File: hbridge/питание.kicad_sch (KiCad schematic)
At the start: 8 parts, among them J19 24V, U14 AMS1117 3.3, U20 B2412S-2WR3, U4 AM6TW-2415DZ, U9 AM6TW-2415DZ

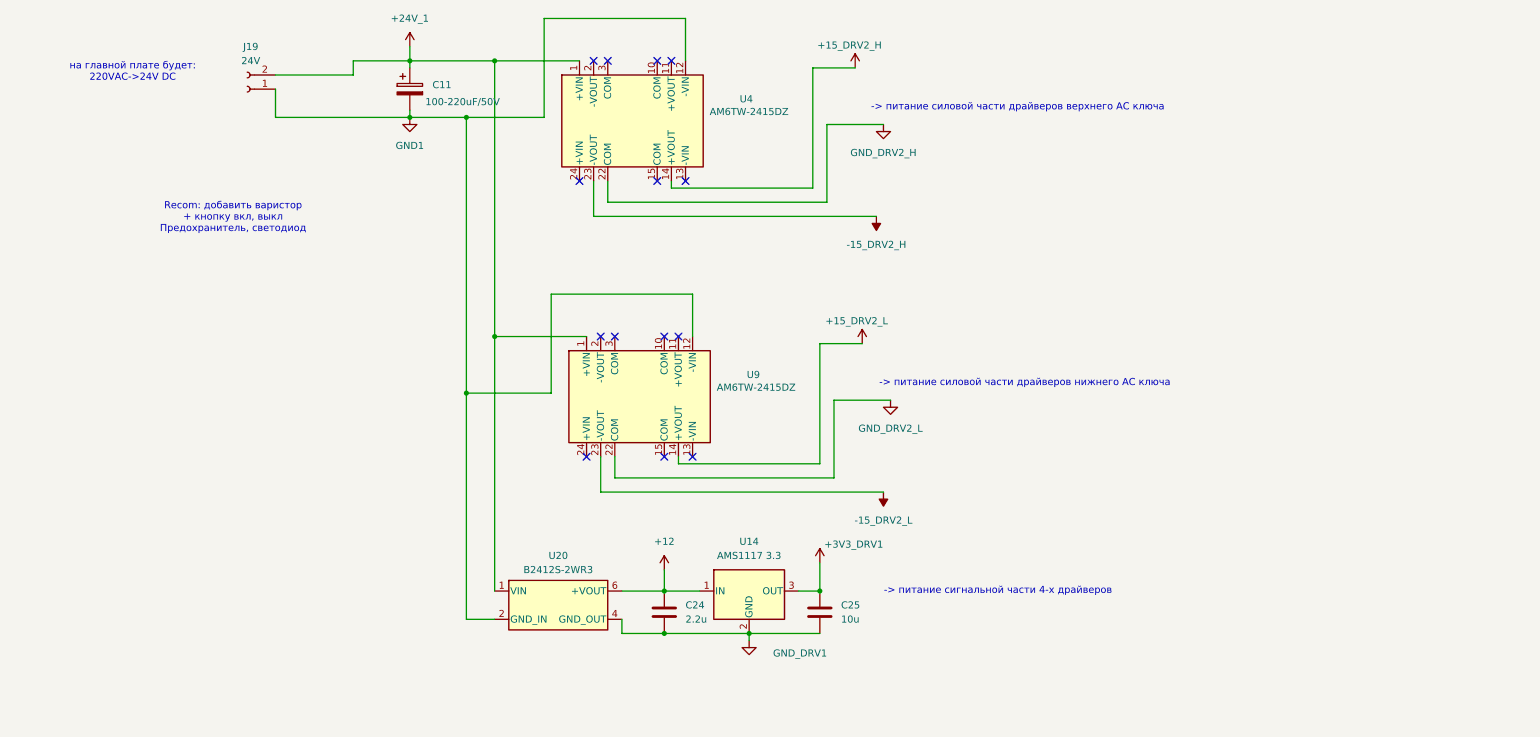
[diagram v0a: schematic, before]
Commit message: Half bridge power to PCB added.
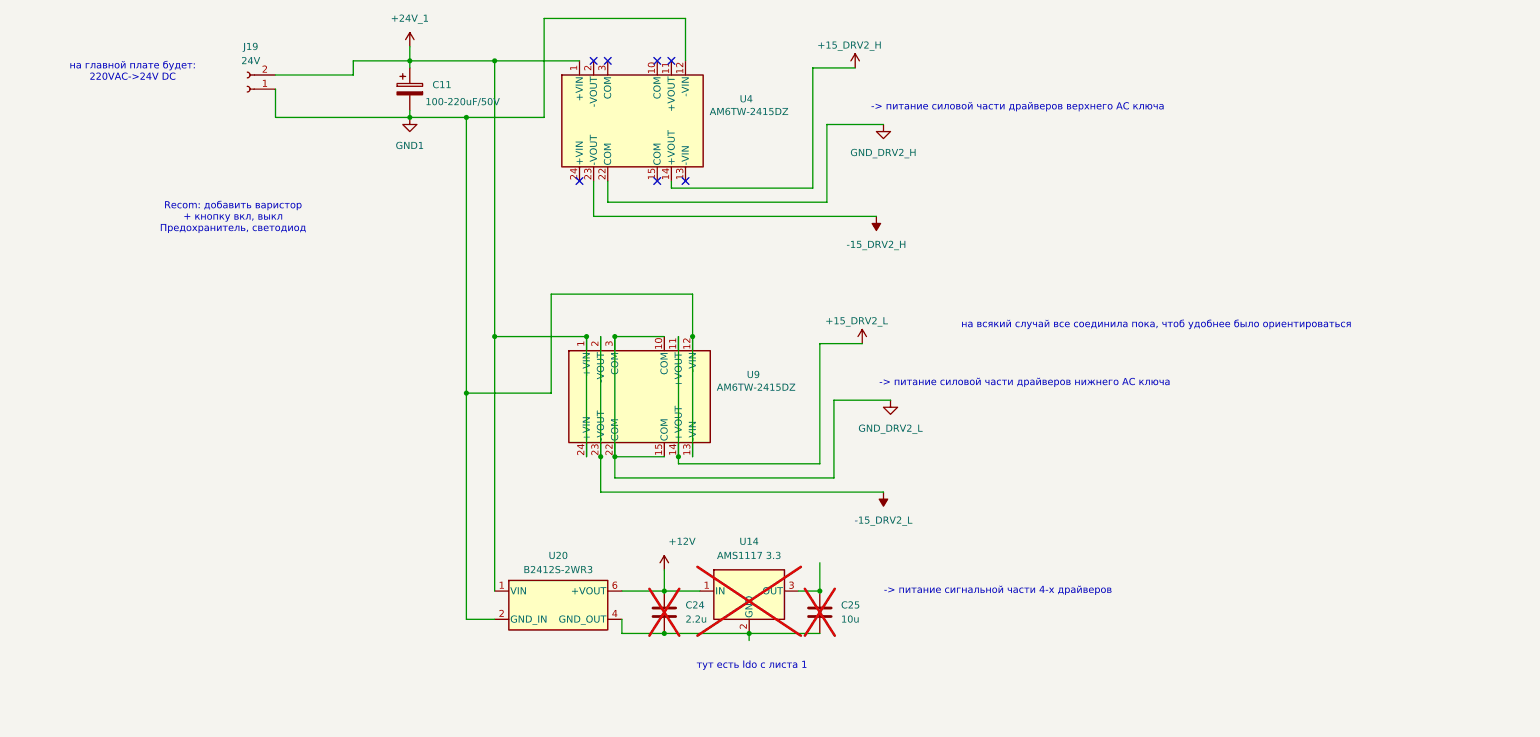
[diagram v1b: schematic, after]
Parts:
- C11: footprint (none) -> Capacitor_THT:CP_Radial_D7.5mm_P2.50mm
- C24, C25: footprint (none) -> Capacitor_SMD:C_0805_2012Metric_Pad1.18x1.45mm_HandSolder; now not fitted; now left out of the parts list
- J19: footprint TerminalBlock_Phoenix:TerminalBlock_Phoenix_MPT-0,5-2-2.54_1x02_P2.54mm_Horizontal -> TerminalBlock:TerminalBlock_Xinya_XY308-2.54-2P_1x02_P2.54mm_Horizontal
- U14: footprint (none) -> Package_TO_SOT_SMD:SOT-223; now not fitted; now left out of the parts list
- U20: footprint (none) -> TerminalBlock:TerminalBlock_Xinya_XY308-2.54-6P_1x06_P2.54mm_Horizontal
- U4, U9: footprint (none) -> Package_DIP:DIP-24_18.0mmx34.29mm_W15.24mm_LongPads
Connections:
- net +15_DRV2_L: now also U9.11 (+VOUT)
- net +24V_1: now also U9.24 (+VIN)
- net -15_DRV2_L: now also U9.2 (-VOUT)
- net GND1: now also U9.13 (-VIN)
- net GND_DRV2_L: now also U9.10 (COM), U9.15 (COM), U9.3 (COM)
- net +12 renamed +12V
- net +3V3_DRV1: no longer names the net of C25.1, U14.3 (OUT)
- net GND_DRV1: no longer names the net of C24.2, C25.2, U14.2 (GND), U20.4 (GND_OUT)
- no-connect marks 14 -> 7
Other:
- note added: "на всякий случай все соединила пока, чтоб удобнее было ориентироваться"
- note added: "тут есть ldo с листа 1"

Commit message: Half-bridge, no MCU.
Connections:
- net +15_DRV2_L: no longer U9.14 (+VOUT)
- net +24V_1: no longer U9.1 (+VIN)
- net -15_DRV2_L: no longer U9.23 (-VOUT)
- net GND1: no longer U9.12 (-VIN)
- net GND_DRV2_H: now also U4.3 (COM); no longer U4.22 (COM)
- net GND_DRV2_L: no longer U9.10 (COM), U9.15 (COM), U9.3 (COM)
- net GND_DRV1: now reaches C24.2, C25.2, U14.2 (GND), U20.4 (GND_OUT)
- no-connect marks 7 -> 14
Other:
- note removed: "на всякий случай все соединила пока, чтоб удобнее было ориентироваться"

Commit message: Hierarchy changed. MCU optocouplers started.
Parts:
- renumbered C25 to C2, C24 to C4, U14 to U7
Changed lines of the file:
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@@
 		(instances
 			(project "hbridge"
-				(path "/2ca728bc-601a-44e1-8d59-41d5093f57eb"
+				(path "/96bc687b-1f0f-4b2f-95bf-a0725acd0403/5c304d23-1a3b-43ed-8f7a-219a4f2f60a2"
 					(reference "#PWR08")
 					(unit 1)
@@
 		(instances
 			(project "hbridge"
-				(path "/2ca728bc-601a-44e1-8d59-41d5093f57eb"
+				(path "/96bc687b-1f0f-4b2f-95bf-a0725acd0403/5c304d23-1a3b-43ed-8f7a-219a4f2f60a2"
 					(reference "#PWR083")
 					(unit 1)
@@
 		(instances
 			(project "hbridge"
-				(path "/2ca728bc-601a-44e1-8d59-41d5093f57eb"
+				(path "/96bc687b-1f0f-4b2f-95bf-a0725acd0403/5c304d23-1a3b-43ed-8f7a-219a4f2f60a2"
 					(reference "#PWR011")
 					(unit 1)
@@
 		(instances
 			(project "hbridge"
-				(path "/2ca728bc-601a-44e1-8d59-41d5093f57eb"
+				(path "/96bc687b-1f0f-4b2f-95bf-a0725acd0403/5c304d23-1a3b-43ed-8f7a-219a4f2f60a2"
 					(reference "#PWR082")
 					(unit 1)
@@
 		(dnp yes)
 		(fields_autoplaced yes)
-		(property "Reference" "U14"
+		(property "Reference" "U7"
 			(at 139.7 134.62 0)
 			(show_name no)
@@
 		(instances
 			(project "hbridge"
-				(path "/2ca728bc-601a-44e1-8d59-41d5093f57eb"
-					(reference "U14")
+				(path "/96bc687b-1f0f-4b2f-95bf-a0725acd0403/5c304d23-1a3b-43ed-8f7a-219a4f2f60a2"
+					(reference "U7")
 					(unit 1)
 				)
@@
 		(instances
 			(project "hbridge"
-				(path "/2ca728bc-601a-44e1-8d59-41d5093f57eb"
+				(path "/96bc687b-1f0f-4b2f-95bf-a0725acd0403/5c304d23-1a3b-43ed-8f7a-219a4f2f60a2"
 					(reference "U4")
 					(unit 1)
@@
 		(dnp yes)
 		(fields_autoplaced yes)
-		(property "Reference" "C24"
+		(property "Reference" "C4"
 			(at 128.27 146.0499 0)
 			(show_name no)
@@
 		(instances
 			(project "hbridge"
-				(path "/2ca728bc-601a-44e1-8d59-41d5093f57eb"
-					(reference "C24")
+				(path "/96bc687b-1f0f-4b2f-95bf-a0725acd0403/5c304d23-1a3b-43ed-8f7a-219a4f2f60a2"
+					(reference "C4")
 					(unit 1)
 				)
@@
 		(instances
 			(project "hbridge"
-				(path "/2ca728bc-601a-44e1-8d59-41d5093f57eb"
+				(path "/96bc687b-1f0f-4b2f-95bf-a0725acd0403/5c304d23-1a3b-43ed-8f7a-219a4f2f60a2"
 					(reference "U9")
 					(unit 1)
@@
 		(dnp yes)
 		(fields_autoplaced yes)
-		(property "Reference" "C25"
+		(property "Reference" "C2"
 			(at 156.21 146.0499 0)
 			(show_name no)
@@
 		(instances
 			(project "hbridge"
-				(path "/2ca728bc-601a-44e1-8d59-41d5093f57eb"
-					(reference "C25")
+				(path "/96bc687b-1f0f-4b2f-95bf-a0725acd0403/5c304d23-1a3b-43ed-8f7a-219a4f2f60a2"
+					(reference "C2")
 					(unit 1)
 				)
@@
 		(instances
 			(project "hbridge"
-				(path "/2ca728bc-601a-44e1-8d59-41d5093f57eb"
+				(path "/96bc687b-1f0f-4b2f-95bf-a0725acd0403/5c304d23-1a3b-43ed-8f7a-219a4f2f60a2"
 					(reference "#PWR09")
 					(unit 1)
@@
 		(instances
 			(project "hbridge"
-				(path "/2ca728bc-601a-44e1-8d59-41d5093f57eb"
+				(path "/96bc687b-1f0f-4b2f-95bf-a0725acd0403/5c304d23-1a3b-43ed-8f7a-219a4f2f60a2"
 					(reference "#PWR0117")
 					(unit 1)
@@
 		(instances
 			(project "hbridge"
-				(path "/2ca728bc-601a-44e1-8d59-41d5093f57eb"
+				(path "/96bc687b-1f0f-4b2f-95bf-a0725acd0403/5c304d23-1a3b-43ed-8f7a-219a4f2f60a2"
 					(reference "C11")
 					(unit 1)
@@
 		(instances
 			(project "hbridge"
-				(path "/2ca728bc-601a-44e1-8d59-41d5093f57eb"
+				(path "/96bc687b-1f0f-4b2f-95bf-a0725acd0403/5c304d23-1a3b-43ed-8f7a-219a4f2f60a2"
 					(reference "J19")
 					(unit 1)
@@
 		(instances
 			(project "hbridge"
-				(path "/2ca728bc-601a-44e1-8d59-41d5093f57eb"
+				(path "/96bc687b-1f0f-4b2f-95bf-a0725acd0403/5c304d23-1a3b-43ed-8f7a-219a4f2f60a2"
 					(reference "#PWR010")
 					(unit 1)
@@
 		(instances
 			(project "hbridge"
-				(path "/2ca728bc-601a-44e1-8d59-41d5093f57eb"
+				(path "/96bc687b-1f0f-4b2f-95bf-a0725acd0403/5c304d23-1a3b-43ed-8f7a-219a4f2f60a2"
 					(reference "#PWR01")
 					(unit 1)
@@
 		(instances
 			(project "hbridge"
-				(path "/2ca728bc-601a-44e1-8d59-41d5093f57eb"
+				(path "/96bc687b-1f0f-4b2f-95bf-a0725acd0403/5c304d23-1a3b-43ed-8f7a-219a4f2f60a2"
 					(reference "U20")
 					(unit 1)
@@
 		(instances
 			(project "hbridge"
-				(path "/2ca728bc-601a-44e1-8d59-41d5093f57eb"
+				(path "/96bc687b-1f0f-4b2f-95bf-a0725acd0403/5c304d23-1a3b-43ed-8f7a-219a4f2f60a2"
 					(reference "#PWR02")
 					(unit 1)
@@
 		(instances
 			(project "hbridge"
-				(path "/2ca728bc-601a-44e1-8d59-41d5093f57eb"
+				(path "/96bc687b-1f0f-4b2f-95bf-a0725acd0403/5c304d23-1a3b-43ed-8f7a-219a4f2f60a2"
 					(reference "#PWR043")
 					(unit 1)
@@
 		)
 	)
-	(sheet_instances
-		(path "/"
-			(page "2")
-		)
-	)

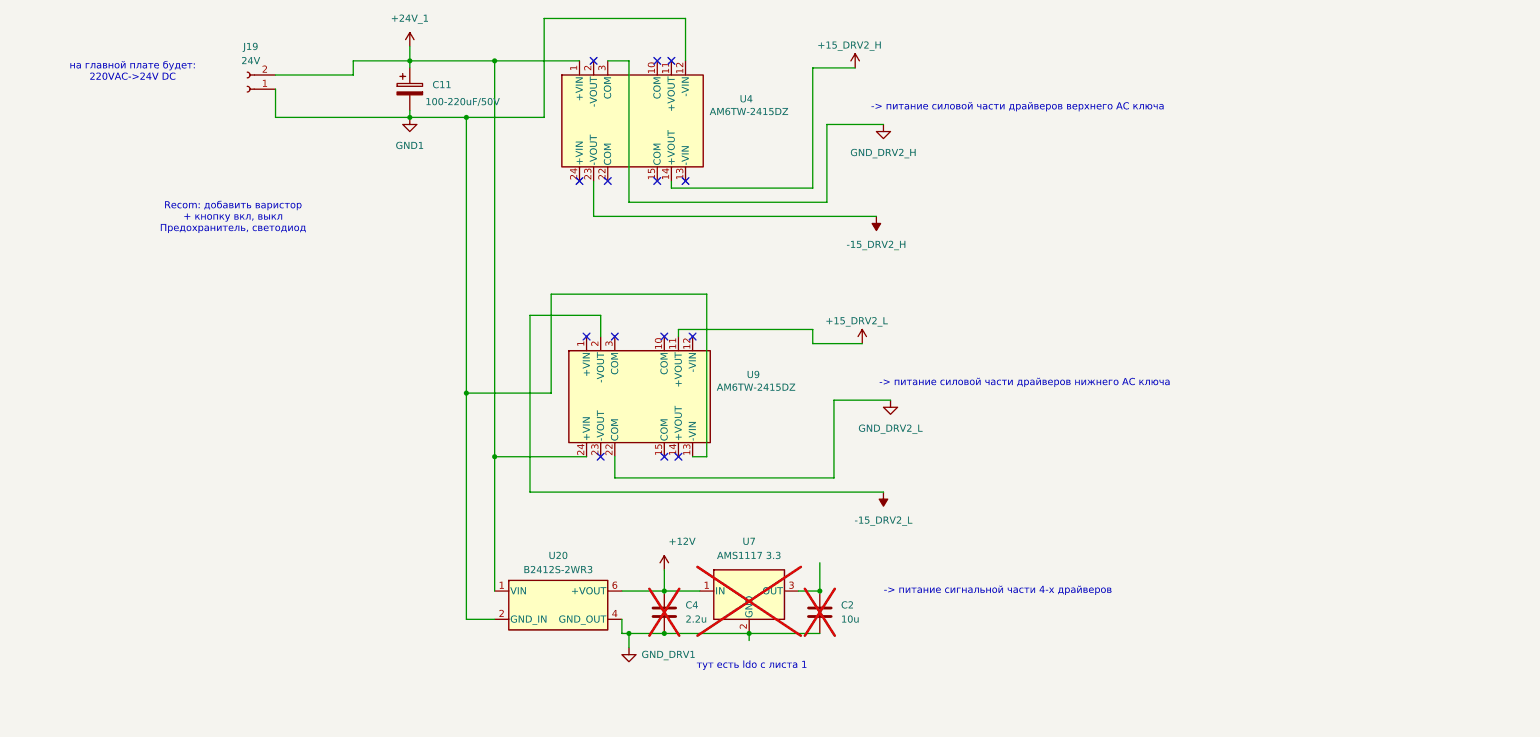
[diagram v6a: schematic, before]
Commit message: Half-bridge refactoring start.
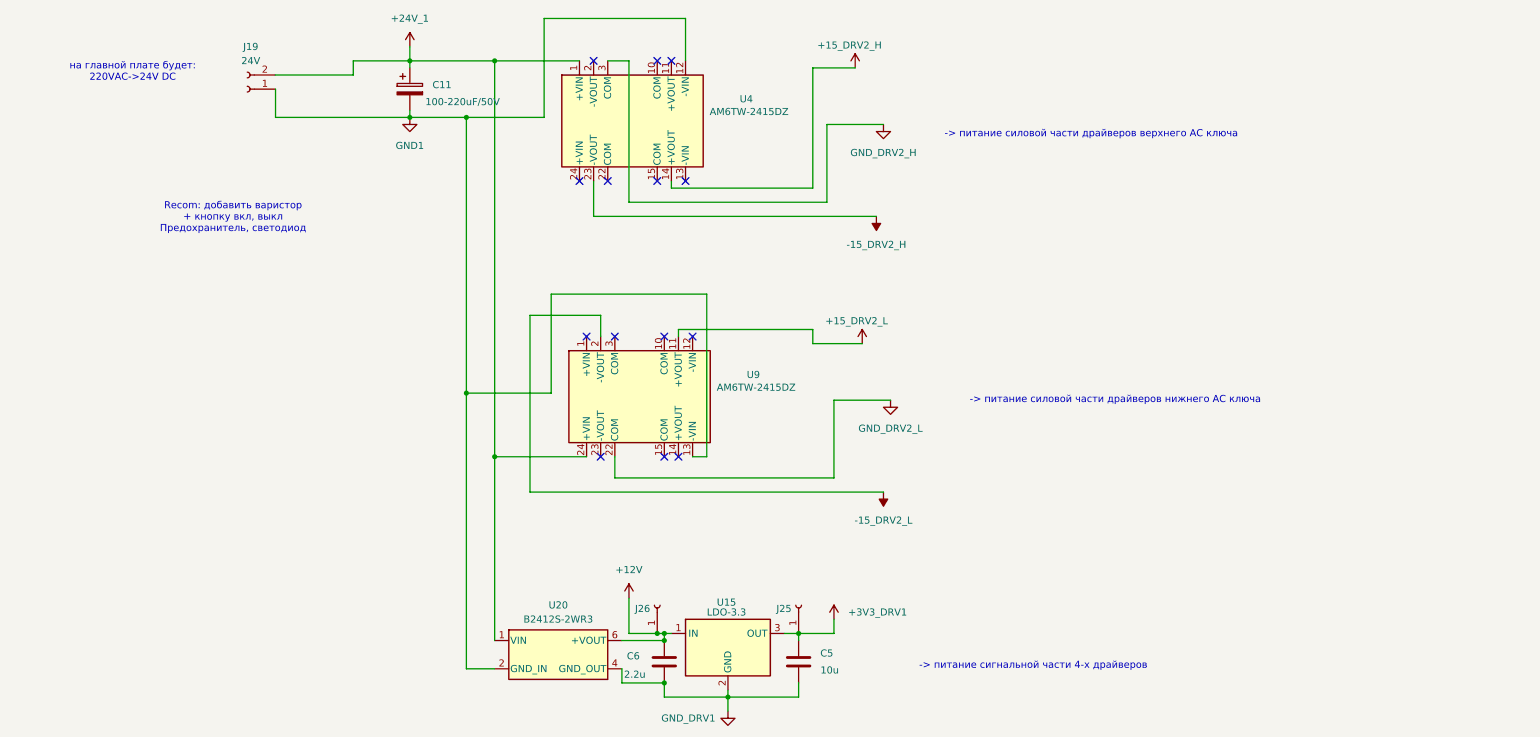
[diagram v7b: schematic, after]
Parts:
- removed C2: 10u, Capacitor_SMD:C_0805_2012Metric_Pad1.18x1.45mm_HandSolder, symbol Device:C
- removed C4: 2.2u, Capacitor_SMD:C_0805_2012Metric_Pad1.18x1.45mm_HandSolder, symbol Device:C
- removed U7: AMS1117 3.3, Package_TO_SOT_SMD:SOT-223, symbol Regulator_Linear:LDK130-ADJ_DFN6
- added C5: 10u, Capacitor_SMD:C_0805_2012Metric_Pad1.18x1.45mm_HandSolder, symbol Device:C
- added C6: 2.2u, Capacitor_SMD:C_0805_2012Metric_Pad1.18x1.45mm_HandSolder, symbol Device:C
- added J25, J26: Conn_01x01_Socket, TestPoint:TestPoint_Loop_D1.80mm_Drill1.0mm_Beaded, symbol Connector:Conn_01x01_Socket
- added U15: LDO-3.3, Package_TO_SOT_SMD:SOT-223-3_TabPin2, symbol Regulator_Linear:LT1963AxST-3.3
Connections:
- net +12V: now also C6.1, J26.1 (Pin_1), U15.1 (IN)
- net GND_DRV1: now also C5.2, C6.2, U15.2 (GND)
- new net +3V3_DRV1: C5.1, J25.1 (Pin_1), U15.3 (OUT)
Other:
- note removed: "тут есть ldo с листа 1"
- moved on the sheet: U20
